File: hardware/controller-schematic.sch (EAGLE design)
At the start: 17 parts, among them IC1 7805TV, Q1 IRLZ44ZV, U1 ATTINY85-20P

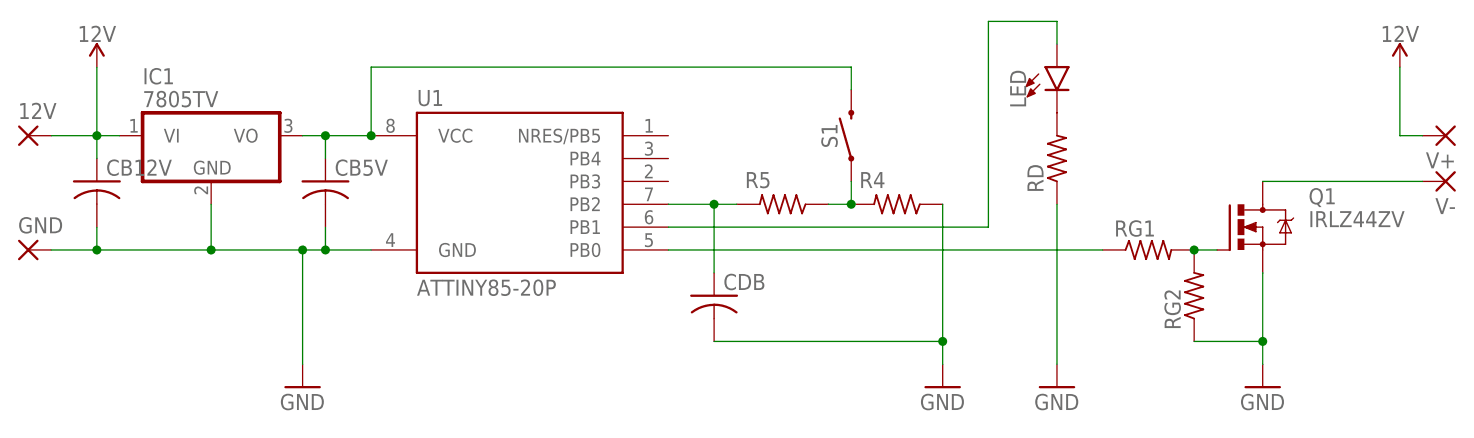
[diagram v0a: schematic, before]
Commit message: Add passives values to schematic and board
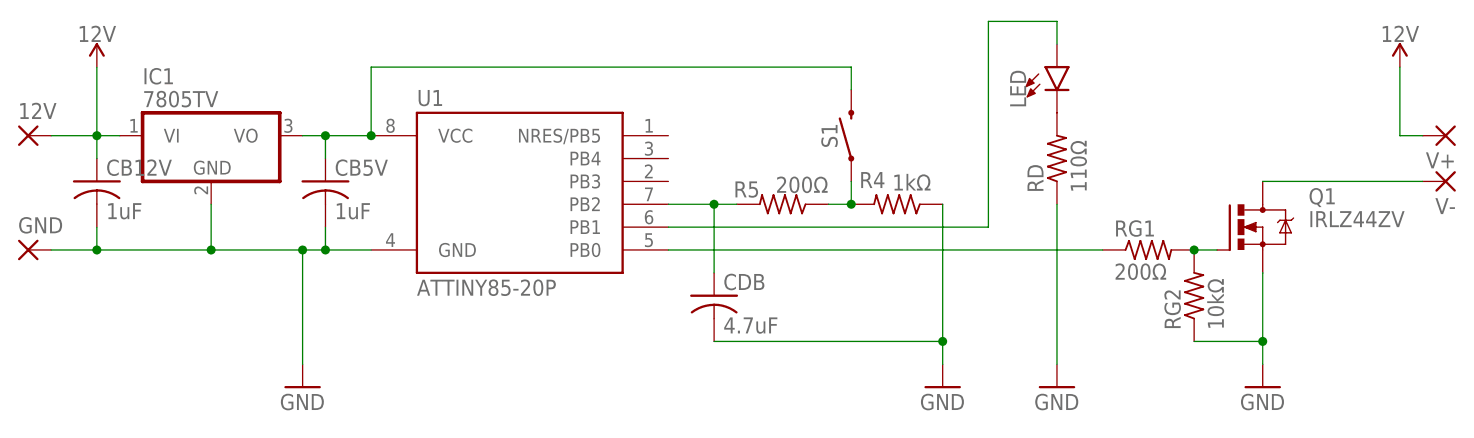
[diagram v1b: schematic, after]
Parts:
- CB12V, CB5V: value (none) -> 1uF
- CDB: value (none) -> 4.7uF
- R4: value (none) -> 1kΩ
- R5, RG1: value (none) -> 200Ω
- RD: value (none) -> 110Ω
- RG2: value (none) -> 10kΩ
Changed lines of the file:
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@@
 <part name="GND" library="wirepad_modified" deviceset="SMD5" device="" package3d_urn="urn:adsk.eagle:package:30841/1"/>
 <part name="GND2" library="supply1" library_urn="urn:adsk.eagle:library:371" deviceset="GND" device=""/>
-<part name="RG1" library="rcl" library_urn="urn:adsk.eagle:library:334" deviceset="R-US_" device="0207/7" package3d_urn="urn:adsk.eagle:package:23493/2"/>
-<part name="RG2" library="rcl" library_urn="urn:adsk.eagle:library:334" deviceset="R-US_" device="0207/7" package3d_urn="urn:adsk.eagle:package:23493/2"/>
+<part name="RG1" library="rcl" library_urn="urn:adsk.eagle:library:334" deviceset="R-US_" device="0207/7" package3d_urn="urn:adsk.eagle:package:23493/2" value="200Ω"/>
+<part name="RG2" library="rcl" library_urn="urn:adsk.eagle:library:334" deviceset="R-US_" device="0207/7" package3d_urn="urn:adsk.eagle:package:23493/2" value="10kΩ"/>
 <part name="V-" library="wirepad_modified" deviceset="SMD5" device="" package3d_urn="urn:adsk.eagle:package:30841/1"/>
 <part name="V+" library="wirepad_modified" deviceset="SMD5" device="" package3d_urn="urn:adsk.eagle:package:30841/1"/>
 <part name="SUPPLY1" library="SparkFun-PowerSymbols" deviceset="12V" device=""/>
 <part name="LED" library="SparkFun-LED" deviceset="LED" device="3MM"/>
-<part name="RD" library="rcl" library_urn="urn:adsk.eagle:library:334" deviceset="R-US_" device="0207/7" package3d_urn="urn:adsk.eagle:package:23493/2"/>
+<part name="RD" library="rcl" library_urn="urn:adsk.eagle:library:334" deviceset="R-US_" device="0207/7" package3d_urn="urn:adsk.eagle:package:23493/2" value="110Ω"/>
 <part name="GND3" library="supply1" library_urn="urn:adsk.eagle:library:371" deviceset="GND" device=""/>
 <part name="S1" library="SparkFun-Switches" deviceset="MOMENTARY-SWITCH-SPST" device="-PTH-6.0MM"/>
 <part name="GND4" library="supply1" library_urn="urn:adsk.eagle:library:371" deviceset="GND" device=""/>
-<part name="R5" library="rcl" library_urn="urn:adsk.eagle:library:334" deviceset="R-US_" device="0207/7" package3d_urn="urn:adsk.eagle:package:23493/2"/>
-<part name="CDB" library="rcl" library_urn="urn:adsk.eagle:library:334" deviceset="C-US" device="050-030X075" package3d_urn="urn:adsk.eagle:package:23640/1"/>
-<part name="R4" library="rcl" library_urn="urn:adsk.eagle:library:334" deviceset="R-US_" device="0207/7" package3d_urn="urn:adsk.eagle:package:23493/2"/>
+<part name="R5" library="rcl" library_urn="urn:adsk.eagle:library:334" deviceset="R-US_" device="0207/7" package3d_urn="urn:adsk.eagle:package:23493/2" value="200Ω"/>
+<part name="CDB" library="rcl" library_urn="urn:adsk.eagle:library:334" deviceset="C-US" device="050-030X075" package3d_urn="urn:adsk.eagle:package:23640/1" value="4.7uF"/>
+<part name="R4" library="rcl" library_urn="urn:adsk.eagle:library:334" deviceset="R-US_" device="0207/7" package3d_urn="urn:adsk.eagle:package:23493/2" value="1kΩ"/>
 <part name="Q1" library="transistor-power" deviceset="IRLZ44Z" device="V" package3d_urn="urn:adsk.eagle:package:29484/3"/>
-<part name="CB5V" library="rcl" library_urn="urn:adsk.eagle:library:334" deviceset="C-US" device="050-030X075" package3d_urn="urn:adsk.eagle:package:23640/1"/>
-<part name="CB12V" library="rcl" library_urn="urn:adsk.eagle:library:334" deviceset="C-US" device="050-030X075" package3d_urn="urn:adsk.eagle:package:23640/1"/>
+<part name="CB5V" library="rcl" library_urn="urn:adsk.eagle:library:334" deviceset="C-US" device="050-030X075" package3d_urn="urn:adsk.eagle:package:23640/1" value="1uF"/>
+<part name="CB12V" library="rcl" library_urn="urn:adsk.eagle:library:334" deviceset="C-US" device="050-030X075" package3d_urn="urn:adsk.eagle:package:23640/1" value="1uF"/>
 </parts>
 <sheets>
@@
 </instance>
 <instance part="R5" gate="G$1" x="139.7" y="71.12" smashed="yes" rot="R180">
-<attribute name="NAME" x="138.43" y="74.7014" size="1.778" layer="95" rot="R180"/>
-<attribute name="VALUE" x="143.51" y="74.422" size="1.778" layer="96" rot="R180"/>
+<attribute name="NAME" x="137.16" y="73.66" size="1.778" layer="95" rot="R180"/>
+<attribute name="VALUE" x="144.78" y="74.168" size="1.778" layer="96" rot="R180"/>
 </instance>
 <instance part="CDB" gate="G$1" x="132.08" y="60.96" smashed="yes">
